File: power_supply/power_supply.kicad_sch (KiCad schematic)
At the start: 30 parts, among them J1 Conn_01x02_Socket, J10 Conn_01x02_Socket, J11 Conn_01x02_Socket, J12 Conn_01x02_Socket, J13 Conn_01x02_Socket, J14 Conn_01x02_Socket, J15 Conn_01x02_Socket, J16 Conn_01x02_Socket, J17 Conn_01x02_Socket, J18 Conn_01x02_Socket, J19 Conn_01x02_Socket, J2 Conn_01x02_Socket, J20 Conn_01x02_Socket, J21 Conn_01x02_Pin, J22 Conn_01x02_Pin, J23 Conn_01x02_Socket, J24 Conn_01x02_Socket, J3 Conn_01x02_Socket, J4 Conn_01x02_Socket, J5 Conn_01x02_Socket, J6 Conn_01x02_Socket, J7 Conn_01x02_Socket, J8 Conn_01x02_Socket, J9 Conn_01x02_Socket

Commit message: 2024/11/05/23:24
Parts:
- removed C1: C, Connector_PinHeader_2.54mm:PinHeader_2x01_P2.54mm_Vertical, symbol Device:C
- removed J10, J11, J12, J13, J14, J15, J16, J17, J18, J19, J20, J6, J7, J8, J9: Conn_01x02_Socket, Connector_JST:JST_XH_B2B-XH-A_1x02_P2.50mm_Vertical, symbol Connector:Conn_01x02_Socket
- removed J21, J22: Conn_01x02_Pin, Connector_AMASS:AMASS_XT60-F_1x02_P7.20mm_Vertical, symbol Connector:Conn_01x02_Pin
- removed J23, J24, J3, J4, J5: Conn_01x02_Socket, Connector_AMASS:AMASS_XT60-F_1x02_P7.20mm_Vertical, symbol Connector:Conn_01x02_Socket
- removed R1: 10, Resistor_THT:R_Axial_DIN0207_L6.3mm_D2.5mm_P10.16mm_Horizontal, symbol Device:R
- removed U1: ~, Connector_PinSocket_2.54mm:PinSocket_1x03_P2.54mm_Vertical, symbol 00_a:LXDC55
- removed U3: ~, footprints:3557-15_KEY, symbol 00_a:fuse
- removed U4: ~, 00a:1MS1-T1-B1-M1-Q-N-S, symbol 00_a:Switch(1MS1-T1-B1-M1-Q-N)
- removed U5: ~, Connector_PinHeader_2.54mm:PinHeader_1x03_P2.54mm_Vertical, symbol 00_a:voltmeter-Red(4530)
- added U1: NJM7805SDL1, Converter_DCDC:Converter_DCDC_NJM7805FA, symbol 00a:3pin_regulator
- added U2: NJM2845DL1-33, Converter_DCDC:Converter_DCDC_NJM7805FA, symbol 00a:3pin_regulator
- J1: value Conn_01x02_Socket -> XT60; footprint Connector_AMASS:AMASS_XT60-F_1x02_P7.20mm_Vertical -> (none)
- J2: value Conn_01x02_Socket -> XT90; footprint Connector_JST:JST_XH_B2B-XH-A_1x02_P2.50mm_Vertical -> (none)
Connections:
- net GND: now also J2.1 (Pin_1); no longer J2.2 (Pin_2)
- net +12V_3 renamed VDD
- net VDD: now also J2.2 (Pin_2)

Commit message: 2024/11/08
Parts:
- added C1, C2, C3, C4: C_Polarized, Capacitor_THT:CP_Radial_D10.0mm_P5.00mm, symbol Device:C_Polarized
- added C5, C7: 0.33μF, Capacitor_SMD:C_0603_1608Metric_Pad1.08x0.95mm_HandSolder, symbol Device:C
- added C6, C8: 0.1μF, Capacitor_SMD:C_0603_1608Metric_Pad1.08x0.95mm_HandSolder, symbol Device:C
- added D1, D2, D3: LED, LED_SMD:LED_0603_1608Metric_Pad1.05x0.95mm_HandSolder, symbol Device:LED
- added D4: OSHR1608C1A, LED_SMD:LED_0603_1608Metric_Pad1.05x0.95mm_HandSolder, symbol Device:LED
- added D5: GS1010FL, Diode_SMD:Nexperia_CFP3_SOD-123W, symbol Device:D
- added D6, D7, D8: D, Diode_THT:D_5W_P12.70mm_Horizontal, symbol Device:D
- added J10, J11, J12, J13, J14, J15, J16, J9: XH_OUT, Connector_JST:JST_XH_B2B-XH-A_1x02_P2.50mm_Vertical, symbol Connector:Conn_01x02_Socket
- added J17, J18, J19, J20, J21, J22, J23, J24: XH_3.3V_OUT, Connector_JST:JST_XH_B2B-XH-A_1x02_P2.50mm_Vertical, symbol Connector:Conn_01x02_Socket
- added J3, J4, J5, J6, J7, J8: XT60_OUT, Connector_AMASS:AMASS_XT60-F_1x02_P7.20mm_Vertical, symbol Connector:Conn_01x02_Socket
- added Q1: 2SC945L-K-T92-K, Package_TO_SOT_THT:TO-92_Inline, symbol Transistor_BJT:BF199
- added R1, R4, R5: 1kΩ, Resistor_SMD:R_0603_1608Metric_Pad0.98x0.95mm_HandSolder, symbol Device:R
- added R2: 300Ω, Resistor_SMD:R_0603_1608Metric_Pad0.98x0.95mm_HandSolder, symbol Device:R
- added R3: 120Ω, Resistor_SMD:R_0603_1608Metric_Pad0.98x0.95mm_HandSolder, symbol Device:R
- added R6: 10kΩ, Resistor_SMD:R_0603_1608Metric_Pad0.98x0.95mm_HandSolder, symbol Device:R
- added SW1: SW_DIP_x04, 00a:KSD42, symbol Switch:SW_DIP_x04
- added U3: 953-1C-12DG-1, 00a:953-1C-12DG-1, symbol 00a:953-1C-12DG-1
- added U4, U5: Y14H-1C-5DS, 00a:Y14H-1C-5DS, symbol 00a:Y14H-1C-5DS
- J1: value XT60 -> XT60_IN; footprint (none) -> Connector_AMASS:AMASS_XT60-F_1x02_P7.20mm_Vertical
- J2: value XT90 -> Emergency Stop Switch; footprint (none) -> Connector_JST:JST_XH_B2B-XH-A_1x02_P2.50mm_Vertical
- U1, U2: footprint Converter_DCDC:Converter_DCDC_NJM7805FA -> 00a:TO-252-3_TabPin2
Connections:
- net GND: now also U1.2 (GND), U2.2 (GND), C1.2, C2.2, C3.2, C4.2, C5.2, C6.2, C7.2, C8.2, D1.1 (K), D2.1 (K), D3.1 (K), J10.2 (Pin_2), J11.2 (Pin_2), J12.2 (Pin_2), J13.2 (Pin_2), J14.2 (Pin_2), J15.2 (Pin_2), J16.2 (Pin_2), J17.2 (Pin_2), J18.2 (Pin_2), J19.2 (Pin_2), J20.2 (Pin_2), J21.2 (Pin_2), J22.2 (Pin_2), J23.2 (Pin_2), J24.2 (Pin_2), J3.1 (Pin_1), J4.1 (Pin_1), J5.1 (Pin_1), J6.1 (Pin_1), J7.1 (Pin_1), J8.1 (Pin_1), J9.2 (Pin_2), Q1.2 (E), R6.1, U4.4 (L2), U5.4 (L2); no longer J2.1 (Pin_1)
- net +12V_IN: now reaches U1.1 (IN)
- net +12V_IN: now also J1.2 (Pin_2), C1.1, C2.1, C3.1, C4.1, C5.1, D4.2 (A), D5.1 (K), U3.1 (VCC)
- net +5V_IN: now reaches U1.3 (OUT)
- net +5V_IN: now also J2.2 (Pin_2), U2.1 (IN), C6.1, C7.1, SW1.1, SW1.2, SW1.3, SW1.4, U4.5 (IN1)
- net +3.3V_IN: now reaches U2.3 (OUT)
- net +3.3V_IN: now also C8.1, U5.5 (IN1)
- removed net VDD: J1.2 (Pin_2), J2.2 (Pin_2)
- new net: D1.2 (A), R1.1
- new net: D8.1 (K), SW1.6, U5.3 (L1)
- new net: D4.1 (K), R4.1
- new net: D5.2 (A), Q1.1 (C), R4.2, U3.2 (SIG)
- new net: D3.2 (A), R3.1
- new net: D6.2 (A), D7.2 (A), D8.2 (A), J2.1 (Pin_1)
- new net: D6.1 (K), R5.1, SW1.8
- new net: D2.2 (A), R2.1
- new net: D7.1 (K), SW1.7, U4.3 (L1)
- new net: Q1.3 (B), R5.2, R6.2
- new net +12V_OUT: J3.2 (Pin_2), J4.2 (Pin_2), J5.2 (Pin_2), J6.2 (Pin_2), J7.2 (Pin_2), J8.2 (Pin_2), R1.2, U3.5 (N.C.)
- new net +12_IN: U3.3 (COM)
- new net +3.3V_OUT: J17.1 (Pin_1), J18.1 (Pin_1), J19.1 (Pin_1), J20.1 (Pin_1), J21.1 (Pin_1), J22.1 (Pin_1), J23.1 (Pin_1), J24.1 (Pin_1), R3.2, U5.1 (N.C.)
- new net +5V_OUT: J10.1 (Pin_1), J11.1 (Pin_1), J12.1 (Pin_1), J13.1 (Pin_1), J14.1 (Pin_1), J15.1 (Pin_1), J16.1 (Pin_1), J9.1 (Pin_1), R2.2, U4.1 (N.C.)
- no-connect marks 0 -> 5
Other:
- moved on the sheet: J1, U1, U2

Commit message: 2024/11/18
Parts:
- removed Q1: 2SC945L-K-T92-K, Package_TO_SOT_THT:TO-92_Inline, symbol Transistor_BJT:BF199
- removed U4, U5: Y14H-1C-5DS, 00a:Y14H-1C-5DS, symbol 00a:Y14H-1C-5DS
- added Q1: TTC014, 00a:TO-252-3_TabPin2, symbol Simulation_SPICE:NPN
- added U4, U5: 134-1C-12DS, 00a:134-1C-12DS, symbol 00_a:134-1C-12DS
- D5: footprint Diode_SMD:Nexperia_CFP3_SOD-123W -> Diode_SMD:D_SOD-123F
- D6, D7, D8: footprint Diode_THT:D_5W_P12.70mm_Horizontal -> Diode_SMD:D_SOD-123F
- J1: footprint Connector_AMASS:AMASS_XT60-F_1x02_P7.20mm_Vertical -> Connector_AMASS:AMASS_XT60-M_1x02_P7.20mm_Vertical
- R1, R4: value 1kΩ -> 10kΩ
- R2: value 300Ω -> 10kΩ
- R3: value 120Ω -> 10kΩ
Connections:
- net +12_IN is gone; now on net +12V_IN: U3.3 (COM)
- net +12V_IN: now also J2.2 (Pin_2), SW1.1, SW1.2, SW1.3, SW1.4
- net +3.3V_IN: now also U5.2
- net +3.3V_OUT: now also U5.3
- net +5V_IN: now also U4.2; no longer J2.2 (Pin_2), SW1.1, SW1.2, SW1.3, SW1.4
- net +5V_OUT: now also U4.3
- net GND: now also Q1.3 (E), U4.4, U5.4
- net at D8.1 (K), SW1.6: now also U5.1
- net at D5.2 (A), R4.2, U3.2 (SIG): now also Q1.2 (C)
- net at D7.1 (K), SW1.7: now also U4.1
- net at R5.2, R6.2: now also Q1.1 (B)
- no-connect marks 5 -> 4

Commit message: 2024/11/19
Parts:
- removed C2, C3, C4: C_Polarized, Capacitor_THT:CP_Radial_D10.0mm_P5.00mm, symbol Device:C_Polarized
- added F1, F2, F3, F4, F5, F6, F7: Fuse, 00a:3557-15_KEY, symbol Device:Fuse
- added J25: XT60_OUT, Connector_AMASS:AMASS_XT60-F_1x02_P7.20mm_Vertical, symbol Connector:Conn_01x02_Socket
- added JP1, JP2, JP3, JP4, JP5, JP6, JP7: SolderJumper_2_Open, Jumper:SolderJumper-2_P1.3mm_Open_Pad1.0x1.5mm, symbol Jumper:SolderJumper_2_Open
- C5, C7: value 0.33μF -> 1μF
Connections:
- net +12V_IN: no longer C1.1
- net +12V_OUT: now also C1.1, F1.1, F2.1, F3.1, F4.1, F5.2, F6.2, F7.2, JP1.1 (A), JP2.1 (A), JP3.1 (A), JP4.1 (A), JP5.1 (A), JP6.1 (A), JP7.1 (A); no longer J3.2 (Pin_2), J4.2 (Pin_2), J5.2 (Pin_2), J6.2 (Pin_2), J7.2 (Pin_2), J8.2 (Pin_2)
- net GND: now also J25.1 (Pin_1)
- new net XT_OUT_1: F1.2, J3.2 (Pin_2), JP1.2 (B)
- new net XT_OUT_2: F2.2, J4.2 (Pin_2), JP2.2 (B)
- new net XT_OUT_3: F3.2, J5.2 (Pin_2), JP3.2 (B)
- new net XT_OUT_4: F4.2, J6.2 (Pin_2), JP4.2 (B)
- new net XT_OUT_5: F5.1, J7.2 (Pin_2), JP5.2 (B)
- new net XT_OUT_6: F6.1, J8.2 (Pin_2), JP6.2 (B)
- new net XT_OUT_7: F7.1, J25.2 (Pin_2), JP7.2 (B)
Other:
- moved on the sheet: J3, J4, J5, J6, J7, J8

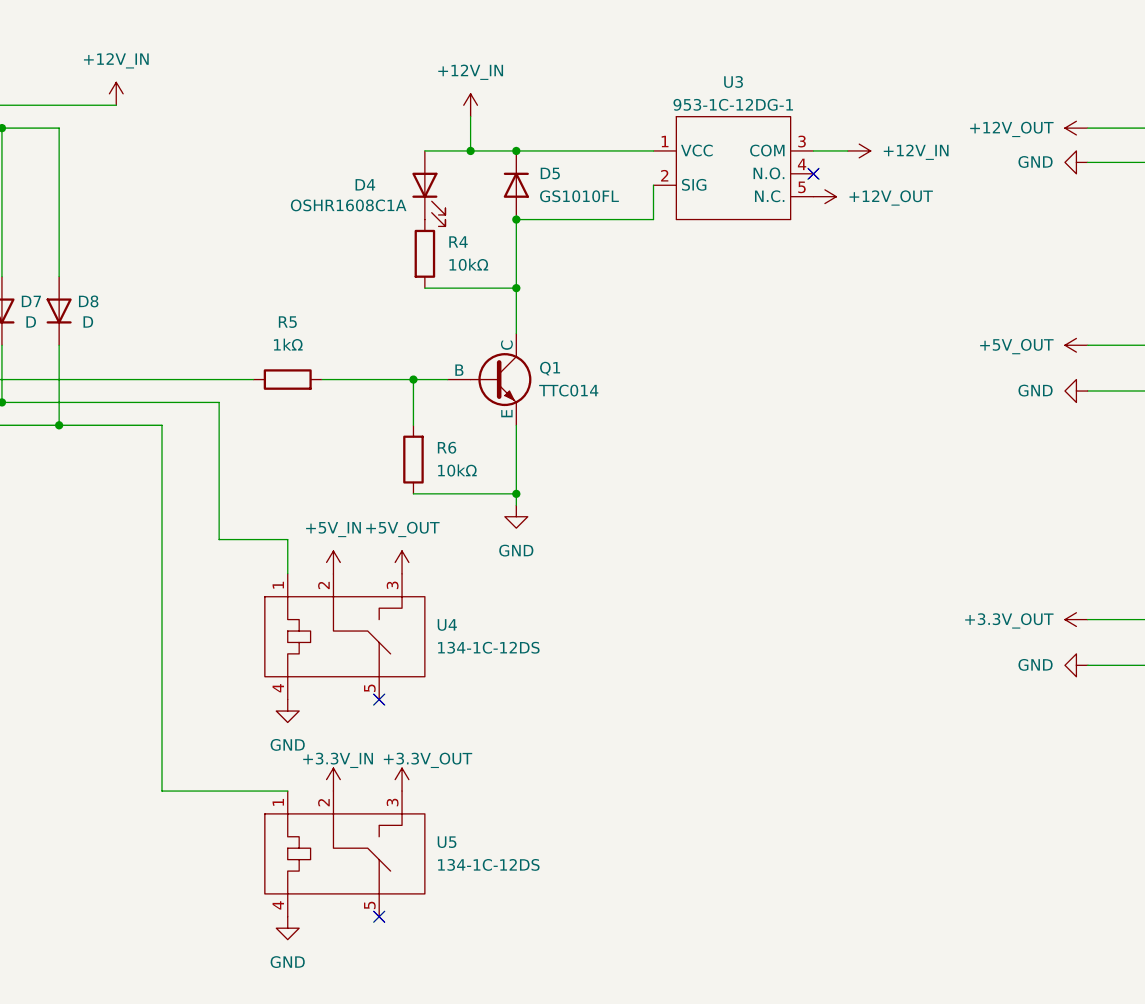
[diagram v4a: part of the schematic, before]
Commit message: 逆起電力用ダイオード追加,小型リレーのフットプリント修正,大型リレーのスイッチを反転
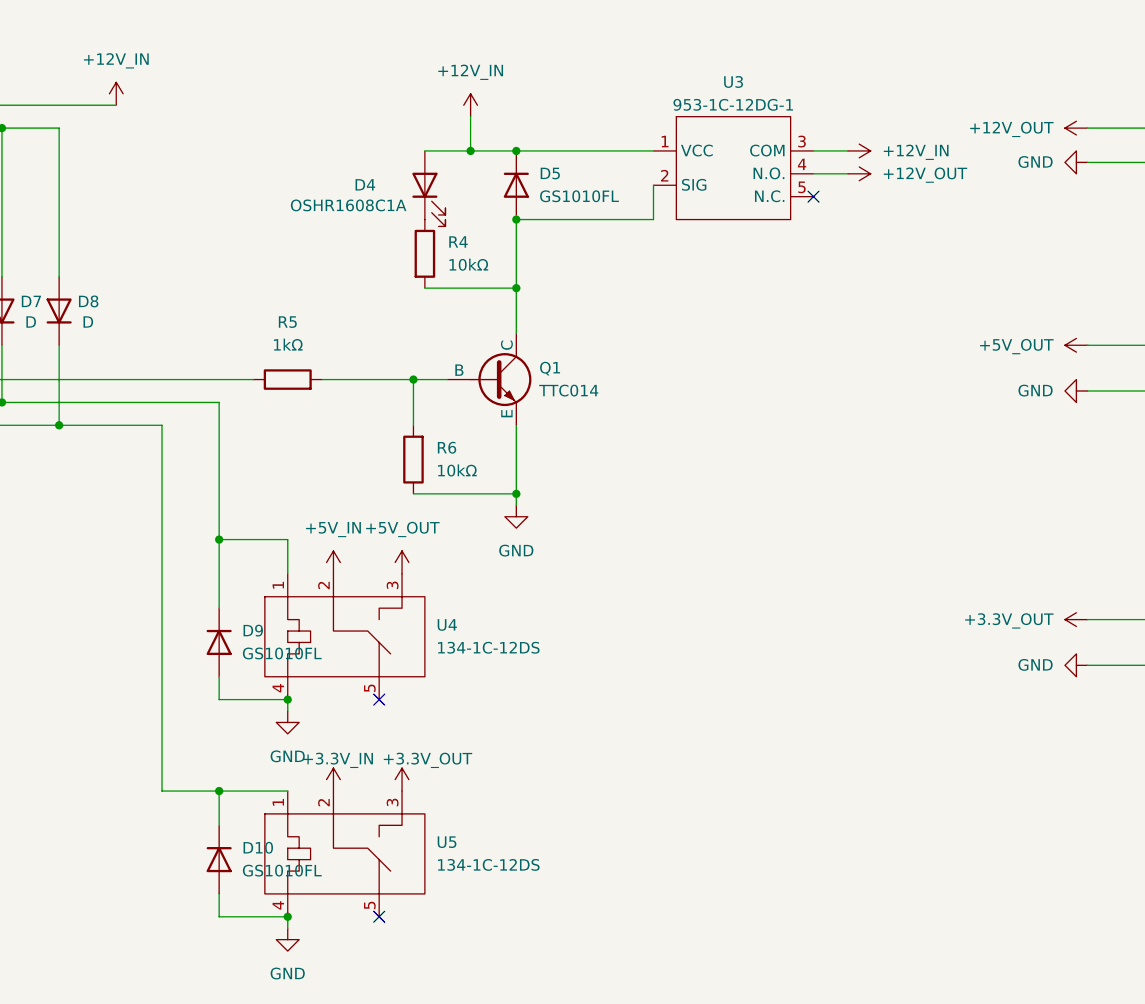
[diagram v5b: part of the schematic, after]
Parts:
- added D10, D9: GS1010FL, Diode_SMD:D_SOD-123F, symbol Device:D
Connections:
- net +12V_OUT: now also U3.4 (N.O.); no longer U3.5 (N.C.)
- net GND: now also D10.2 (A), D9.2 (A)
- net at D8.1 (K), SW1.6, U5.1: now also D10.1 (K)
- net at D7.1 (K), SW1.7, U4.1: now also D9.1 (K)
